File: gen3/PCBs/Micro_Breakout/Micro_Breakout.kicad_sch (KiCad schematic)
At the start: 46 parts, among them J1 430450422, J10 430450228, J11 430450422, J12 430450228, J13 430450228, J14 Conn_01x03_Pin, J15 430450422, J16 430450422, J17 430450422, J18 430450422, J19 Conn_01x10, J2 SBH11-PBPC-D05-ST-BK, J20 Conn_01x10, J21 Conn_01x10, J22 430450612, J23 430450612, J24 430450612, J25 430450422, J3 Battery, J4 Conn_01x24, J5 Battery, J6 Conn_01x24, J7 430450422, J8 430450422, J9 430450228, Q7 L78M05ABDT-TR, U15 AMS1117-3.3, U2 MCP9808_MSOP, U4 BME280, U6 Teensy4.1

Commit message: microcontroller breakout board completed!!
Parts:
- added H6, H7, H8, H9: MountingHole, MountingHole:MountingHole_4.3mm_M4, symbol Mechanical:MountingHole
- J1: value 430450422 -> BlueRobotics Depth Sensor
- J10: value 430450228 -> Kill Switch
- J11: value 430450422 -> StarOddi CTD Comms
- J12: value 430450228 -> LED1
- J13: value 430450228 -> LED2
- J14: value Conn_01x03_Pin -> Leak Sensor
- J15: value 430450422 -> Extra I2C #3
- J16: value 430450422 -> Extra I2C #6
- J17: value 430450422 -> Extra I2C #5
- J18: value 430450422 -> Extra I2C #4
- J19: value Conn_01x10 -> GND Line
- J2: value SBH11-PBPC-D05-ST-BK -> Interconnect
- J20: value Conn_01x10 -> 3.3V Line
- J21: value Conn_01x10 -> 5V Line
- J22: value 430450612 -> Extra SPI #1
- J23: value 430450612 -> Extra SPI #2
- J24: value 430450612 -> Extra SPI #3
- J25: value 430450422 -> Secondary UART
- J3: value Battery -> External Battery
- J5: value Battery -> External I2C
- J7: value 430450422 -> Extra I2C #1
- J8: value 430450422 -> Extra I2C #2
- J9: value 430450228 -> Lumen PWM
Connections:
- net +3.3V: now also J25.4
- net Dled1: now also J4.16 (Pin_16); no longer J4.17 (Pin_17)
- net Dled2: now also J4.17 (Pin_17); no longer J4.16 (Pin_16)
- net GND: now also J25.2
- net UART_RX2: now also J25.1
- net UART_TX2: now also J25.3
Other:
- moved on the sheet: J2, J25, R7, R8

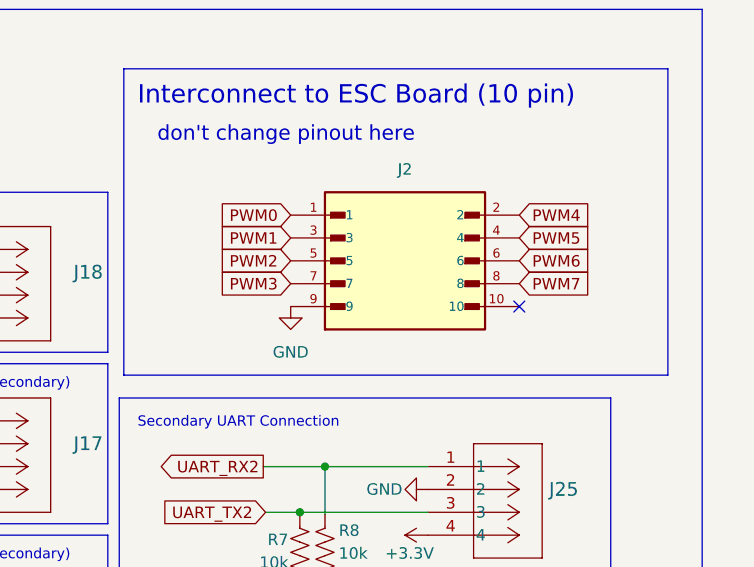
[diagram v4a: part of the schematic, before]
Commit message: fixed pinout for ribbon
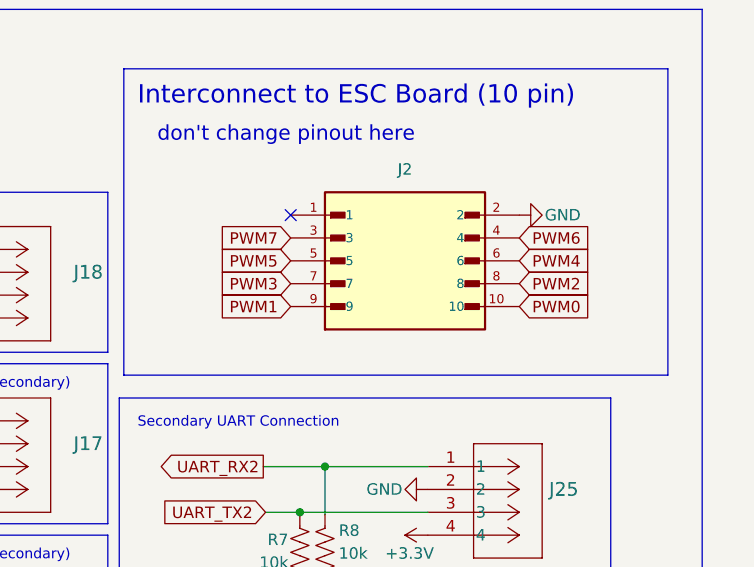
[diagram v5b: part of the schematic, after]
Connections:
- net GND: now also J2.2; no longer J2.9
- net PWM0: now also J2.10; no longer J2.1
- net PWM1: now also J2.9; no longer J2.3
- net PWM2: now also J2.8; no longer J2.5
- net PWM4: now also J2.6; no longer J2.2
- net PWM5: now also J2.5; no longer J2.4
- net PWM6: now also J2.4; no longer J2.6
- net PWM7: now also J2.3; no longer J2.8
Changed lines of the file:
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@@
 	)
 	(no_connect
+		(at 345.44 176.53)
+	)
+	(no_connect
 		(at 73.66 109.22)
 	)
@@
 	)
 	(no_connect
-		(at 370.84 186.69)
-	)
-	(no_connect
 		(at 69.85 109.22)
 	)
@@
 	(global_label "PWM1"
 		(shape input)
-		(at 345.44 179.07 180)
+		(at 345.44 186.69 180)
 		(fields_autoplaced yes)
 		(effects
@@
 		)
 		(property "Intersheetrefs" "${INTERSHEET_REFS}"
-			(at 337.0725 179.07 0)
+			(at 337.0725 186.69 0)
 			(effects
 				(font
@@
 	(global_label "PWM2"
 		(shape input)
-		(at 345.44 181.61 180)
+		(at 370.84 184.15 0)
 		(fields_autoplaced yes)
 		(effects
@@
 				(size 1.27 1.27)
 			)
-			(justify right)
+			(justify left)
 		)
 		(property "Intersheetrefs" "${INTERSHEET_REFS}"
-			(at 337.0725 181.61 0)
+			(at 379.2075 184.15 0)
 			(effects
 				(font
 					(size 1.27 1.27)
 				)
-				(justify right)
+				(justify left)
 				(hide yes)
 			)
@@
 	(global_label "PWM5"
 		(shape input)
-		(at 370.84 179.07 0)
+		(at 345.44 181.61 180)
 		(fields_autoplaced yes)
 		(effects
@@
 				(size 1.27 1.27)
 			)
-			(justify left)
+			(justify right)
 		)
 		(property "Intersheetrefs" "${INTERSHEET_REFS}"
-			(at 379.2075 179.07 0)
+			(at 337.0725 181.61 0)
 			(effects
 				(font
 					(size 1.27 1.27)
 				)
-				(justify left)
+				(justify right)
 				(hide yes)
 			)
@@
 	(global_label "PWM0"
 		(shape input)
-		(at 345.44 176.53 180)
+		(at 370.84 186.69 0)
 		(fields_autoplaced yes)
 		(effects
@@
 				(size 1.27 1.27)
 			)
-			(justify right)
+			(justify left)
 		)
 		(property "Intersheetrefs" "${INTERSHEET_REFS}"
-			(at 337.0725 176.53 0)
+			(at 379.2075 186.69 0)
 			(effects
 				(font
 					(size 1.27 1.27)
 				)
-				(justify right)
+				(justify left)
 				(hide yes)
 			)
@@
 	(global_label "PWM7"
 		(shape input)
-		(at 370.84 184.15 0)
+		(at 345.44 179.07 180)
 		(fields_autoplaced yes)
 		(effects
@@
 				(size 1.27 1.27)
 			)
-			(justify left)
+			(justify right)
 		)
 		(property "Intersheetrefs" "${INTERSHEET_REFS}"
-			(at 379.2075 184.15 0)
+			(at 337.0725 179.07 0)
 			(effects
 				(font
 					(size 1.27 1.27)
 				)
-				(justify left)
+				(justify right)
 				(hide yes)
 			)
@@
 	(global_label "PWM6"
 		(shape input)
-		(at 370.84 181.61 0)
+		(at 370.84 179.07 0)
 		(fields_autoplaced yes)
 		(effects
@@
 		)
 		(property "Intersheetrefs" "${INTERSHEET_REFS}"
-			(at 379.2075 181.61 0)
+			(at 379.2075 179.07 0)
 			(effects
 				(font
@@
 	(global_label "PWM4"
 		(shape input)
-		(at 370.84 176.53 0)
+		(at 370.84 181.61 0)
 		(fields_autoplaced yes)
 		(effects
@@
 		)
 		(property "Intersheetrefs" "${INTERSHEET_REFS}"
-			(at 379.2075 176.53 0)
+			(at 379.2075 181.61 0)
 			(effects
 				(font
@@
 	)
 	(symbol
-		(lib_id "power:GND")
-		(at 345.44 186.69 0)
-		(unit 1)
-		(exclude_from_sim no)
-		(in_bom yes)
-		(on_board yes)
-		(dnp no)
-		(fields_autoplaced yes)
-		(property "Reference" "#PWR02"
-			(at 345.44 193.04 0)
-			(effects
-				(font
-					(size 1.27 1.27)
-				)
-				(hide yes)
-			)
-		)
-		(property "Value" "GND"
-			(at 345.44 191.77 0)
-			(effects
-				(font
-					(size 1.27 1.27)
-				)
-			)
-		)
-		(property "Footprint" ""
-			(at 345.44 186.69 0)
-			(effects
-				(font
-					(size 1.27 1.27)
-				)
-				(hide yes)
-			)
-		)
-		(property "Datasheet" ""
-			(at 345.44 186.69 0)
-			(effects
-				(font
-					(size 1.27 1.27)
-				)
-				(hide yes)
-			)
-		)
-		(property "Description" "Power symbol creates a global label with name \"GND\" , ground"
-			(at 345.44 186.69 0)
-			(effects
-				(font
-					(size 1.27 1.27)
-				)
-				(hide yes)
-			)
-		)
-		(pin "1"
-		)
-		(instances
-			(project "Micro_Breakout"
-				(path "/55121ba7-5d22-4fe3-93aa-7f76d75b410c"
-					(reference "#PWR02")
-					(unit 1)
-				)
-			)
-		)
-	)
-	(symbol
 		(lib_id "power:+3.3V")
 		(at 309.88 233.68 270)
@@
 					(unit 1)
 				)
+			)
+		)
+	)
+	(symbol
+		(lib_id "power:GND")
+		(at 370.84 176.53 90)
+		(unit 1)
+		(exclude_from_sim no)
+		(in_bom yes)
+		(on_board yes)
+		(dnp no)
+		(property "Reference" "#PWR02"
+			(at 377.19 176.53 0)
+			(effects
+				(font
+					(size 1.27 1.27)
+				)
+				(hide yes)
+			)
+		)
+		(property "Value" "GND"
+			(at 375.666 176.53 90)
+			(effects
+				(font
+					(size 1.27 1.27)
+				)
+			)
+		)
+		(property "Footprint" ""
+			(at 370.84 176.53 0)
+			(effects
+				(font
+					(size 1.27 1.27)
+				)
+				(hide yes)
+			)
+		)
+		(property "Datasheet" ""
+			(at 370.84 176.53 0)
+			(effects
+				(font
+					(size 1.27 1.27)
+				)
+				(hide yes)
+			)
+		)
+		(property "Description" "Power symbol creates a global label with name \"GND\" , ground"
+			(at 370.84 176.53 0)
+			(effects
+				(font
+					(size 1.27 1.27)
+				)
+				(hide yes)
+			)
+		)
+		(pin "1"
+		)
+		(instances
+			(project "Micro_Breakout"
+				(path "/55121ba7-5d22-4fe3-93aa-7f76d75b410c"
+					(reference "#PWR02")
+					(unit 1)
+				)

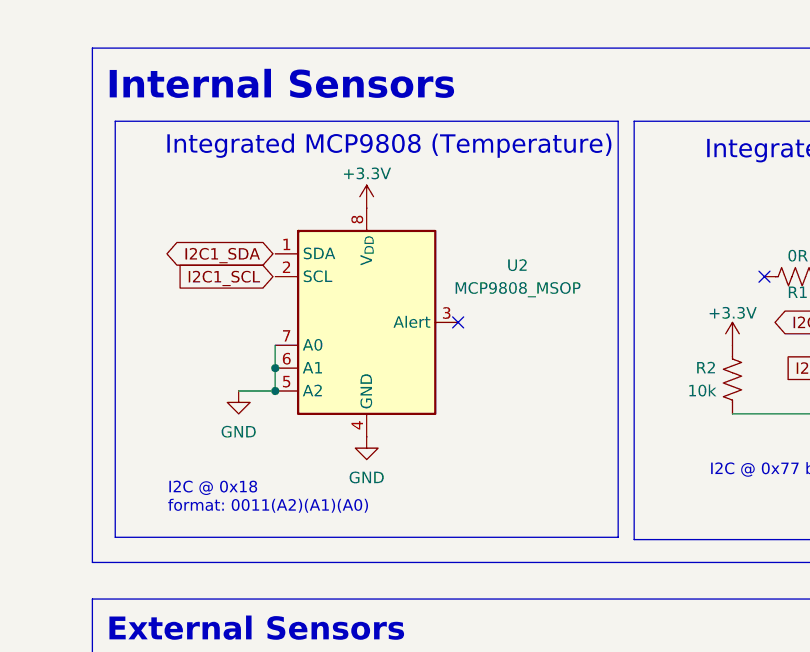
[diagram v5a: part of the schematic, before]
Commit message: connected missing SDA SCL connection on gen 3 micro board
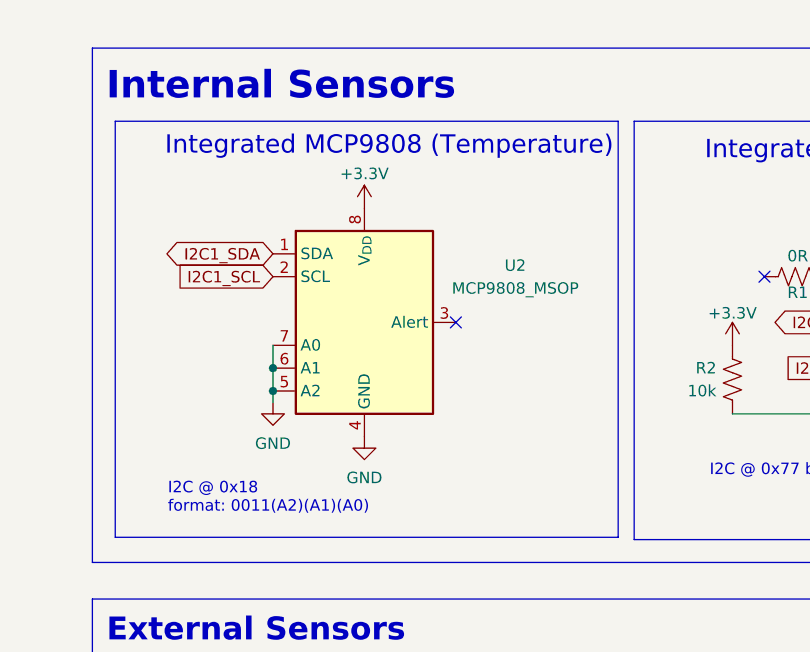
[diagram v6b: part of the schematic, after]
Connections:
- net I2C1_SCL: now also U2.2 (SCL)
- net I2C1_SDA: now also U2.1 (SDA)
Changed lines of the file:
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@@
 	(title_block
 		(title "Main Microcontroller Breakout Board")
-		(date "2026/2/21")
-		(rev "2.0")
+		(date "2026-04-07")
+		(rev "3.0")
 		(company "Stanford Robosub")
 		(comment 1 "Ryota Sato - ryos17@stanford.edu")
@@
 	)
 	(junction
-		(at 346.456 209.55)
+		(at 189.23 57.15)
 		(diameter 0)
 		(color 0 0 0 0)
 	)
 	(junction
-		(at 189.484 59.69)
+		(at 346.456 209.55)
 		(diameter 0)
 		(color 0 0 0 0)
@@
 	)
 	(junction
-		(at 189.484 57.15)
-		(diameter 0)
-		(color 0 0 0 0)
-	)
-	(junction
 		(at 270.51 236.22)
 		(diameter 0)
@@
 	)
 	(junction
+		(at 189.23 59.69)
+		(diameter 0)
+		(color 0 0 0 0)
+	)
+	(junction
 		(at 373.126 77.47)
 		(diameter 0)
@@
 	)
 	(no_connect
-		(at 209.804 52.07)
+		(at 209.55 52.07)
 	)
 	(no_connect
@@
 	(wire
 		(pts
-			(xy 189.484 54.61) (xy 189.484 57.15)
+			(xy 189.23 54.61) (xy 189.23 57.15)
 		)
 		(stroke
@@
 	(wire
 		(pts
+			(xy 189.23 57.15) (xy 189.23 59.69)
+		)
+		(stroke
+			(width 0)
+			(type default)
+		)
+	)
+	(wire
+		(pts
 			(xy 104.14 180.34) (xy 100.33 180.34)
 		)
@@
 	(wire
 		(pts
-			(xy 189.484 57.15) (xy 189.484 59.69)
-		)
-		(stroke
-			(width 0)
-			(type default)
-		)
-	)
-	(wire
-		(pts
 			(xy 283.21 236.22) (xy 285.75 236.22)
 		)
@@
 	(wire
 		(pts
-			(xy 185.42 59.69) (xy 189.484 59.69)
-		)
-		(stroke
-			(width 0)
-			(type default)
-		)
-	)
-	(wire
-		(pts
 			(xy 143.51 190.5) (xy 140.97 190.5)
 		)
@@
 	(wire
 		(pts
+			(xy 189.23 59.69) (xy 189.23 60.96)
+		)
+		(stroke
+			(width 0)
+			(type default)
+		)
+	)
+	(wire
+		(pts
 			(xy 104.14 223.52) (xy 100.33 223.52)
 		)
@@
 	(symbol
 		(lib_id "power:+3.3V")
-		(at 199.644 39.37 0)
+		(at 199.39 39.37 0)
 		(unit 1)
 		(exclude_from_sim no)
@@
 		(dnp no)
 		(property "Reference" "#PWR012"
-			(at 199.644 43.18 0)
+			(at 199.39 43.18 0)
 			(effects
 				(font
@@
 		)
 		(property "Value" "+3.3V"
-			(at 199.644 35.56 0)
+			(at 199.39 35.56 0)
 			(effects
 				(font
@@
 		)
 		(property "Footprint" ""
-			(at 199.644 39.37 0)
+			(at 199.39 39.37 0)
 			(effects
 				(font
@@
 		)
 		(property "Datasheet" ""
-			(at 199.644 39.37 0)
+			(at 199.39 39.37 0)
 			(effects
 				(font
@@
 		)
 		(property "Description" "Power symbol creates a global label with name \"+3.3V\""
-			(at 199.644 39.37 0)
+			(at 199.39 39.37 0)
 			(effects
 				(font
@@
 	(symbol
 		(lib_id "power:GND")
-		(at 185.42 59.69 0)
+		(at 189.23 60.96 0)
 		(unit 1)
 		(exclude_from_sim no)
@@
 		(fields_autoplaced yes)
 		(property "Reference" "#PWR018"
-			(at 185.42 66.04 0)
+			(at 189.23 67.31 0)
 			(effects
 				(font
@@
 		)
 		(property "Value" "GND"
-			(at 185.42 64.262 0)
+			(at 189.23 65.532 0)
 			(effects
 				(font
@@
 		)
 		(property "Footprint" ""
-			(at 185.42 59.69 0)
+			(at 189.23 60.96 0)
 			(effects
 				(font
@@
 		)
 		(property "Datasheet" ""
-			(at 185.42 59.69 0)
+			(at 189.23 60.96 0)
 			(effects
 				(font
@@
 		)
 		(property "Description" "Power symbol creates a global label with name \"GND\" , ground"
-			(at 185.42 59.69 0)
+			(at 189.23 60.96 0)
 			(effects
 				(font
@@
 	(symbol
 		(lib_id "Sensor_Temperature:MCP9808_MSOP")
-		(at 199.644 52.07 0)
+		(at 199.39 52.07 0)
 		(unit 1)
 		(exclude_from_sim no)
@@
 		(fields_autoplaced yes)
 		(property "Reference" "U2"
-			(at 216.408 45.7514 0)
+			(at 216.154 45.7514 0)
 			(effects
 				(font
@@
 		)
 		(property "Value" "MCP9808_MSOP"
-			(at 216.408 48.2914 0)
+			(at 216.154 48.2914 0)
 			(effects
 				(font
@@
 		)
 		(property "Footprint" "Package_SO:MSOP-8_3x3mm_P0.65mm"
-			(at 199.644 52.07 0)
+			(at 199.39 52.07 0)
 			(effects
 				(font
@@
 		)
 		(property "Datasheet" "http://ww1.microchip.com/downloads/en/DeviceDoc/22203b.pdf"
-			(at 193.294 40.64 0)
+			(at 193.04 40.64 0)
 			(effects
 				(font
@@
 		)
 		(property "Description" "±0.25°C (±0.5°C) Typical (Maximum), Digital Temperature Sensor, MSOP-8"
-			(at 199.644 52.07 0)
+			(at 199.39 52.07 0)
 			(effects
 				(font
@@
 		)
 		(property "MFR" ""
-			(at 199.644 52.07 0)
+			(at 199.39 52.07 0)
 			(effects
 				(font
@@
 		)
 		(property "MFR S/N" ""
-			(at 199.644 52.07 0)
+			(at 199.39 52.07 0)
 			(effects
 				(font
@@
 		)
 		(property "Supplier 1" "https://www.digikey.com/en/products/detail/microchip-technology/MCP9808T-E-MS/2803667"
-			(at 199.644 52.07 0)
+			(at 199.39 52.07 0)
 			(effects
 				(font
@@
 		)
 		(property "Supplier 1 S/N" "MCP9808T-E/MSCT-ND"
-			(at 199.644 52.07 0)
+			(at 199.39 52.07 0)
 			(effects
 				(font
@@
 		)
 		(property "Supplier 2" ""
-			(at 199.644 52.07 0)
+			(at 199.39 52.07 0)
 			(effects
 				(font
@@
 		)
 		(property "Supplier 2 S/N" ""
-			(at 199.644 52.07 0)
+			(at 199.39 52.07 0)
 			(effects
 				(font
@@
 	(symbol
 		(lib_id "power:GND")
-		(at 199.644 64.77 0)
+		(at 199.39 64.77 0)
 		(unit 1)
 		(exclude_from_sim no)
@@
 		(fields_autoplaced yes)
 		(property "Reference" "#PWR020"
-			(at 199.644 71.12 0)
+			(at 199.39 71.12 0)
 			(effects
 				(font
@@
 		)
 		(property "Value" "GND"
-			(at 199.644 69.342 0)
+			(at 199.39 69.342 0)
 			(effects
 				(font
@@
 		)
 		(property "Footprint" ""
-			(at 199.644 64.77 0)
+			(at 199.39 64.77 0)
 			(effects
 				(font
@@
 		)
 		(property "Datasheet" ""
-			(at 199.644 64.77 0)
+			(at 199.39 64.77 0)
 			(effects
 				(font
@@
 		)
 		(property "Description" "Power symbol creates a global label with name \"GND\" , ground"
-			(at 199.644 64.77 0)
+			(at 199.39 64.77 0)
 			(effects
 				(font
